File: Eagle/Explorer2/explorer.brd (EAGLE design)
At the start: 101.6 x 66 mm, 12 parts

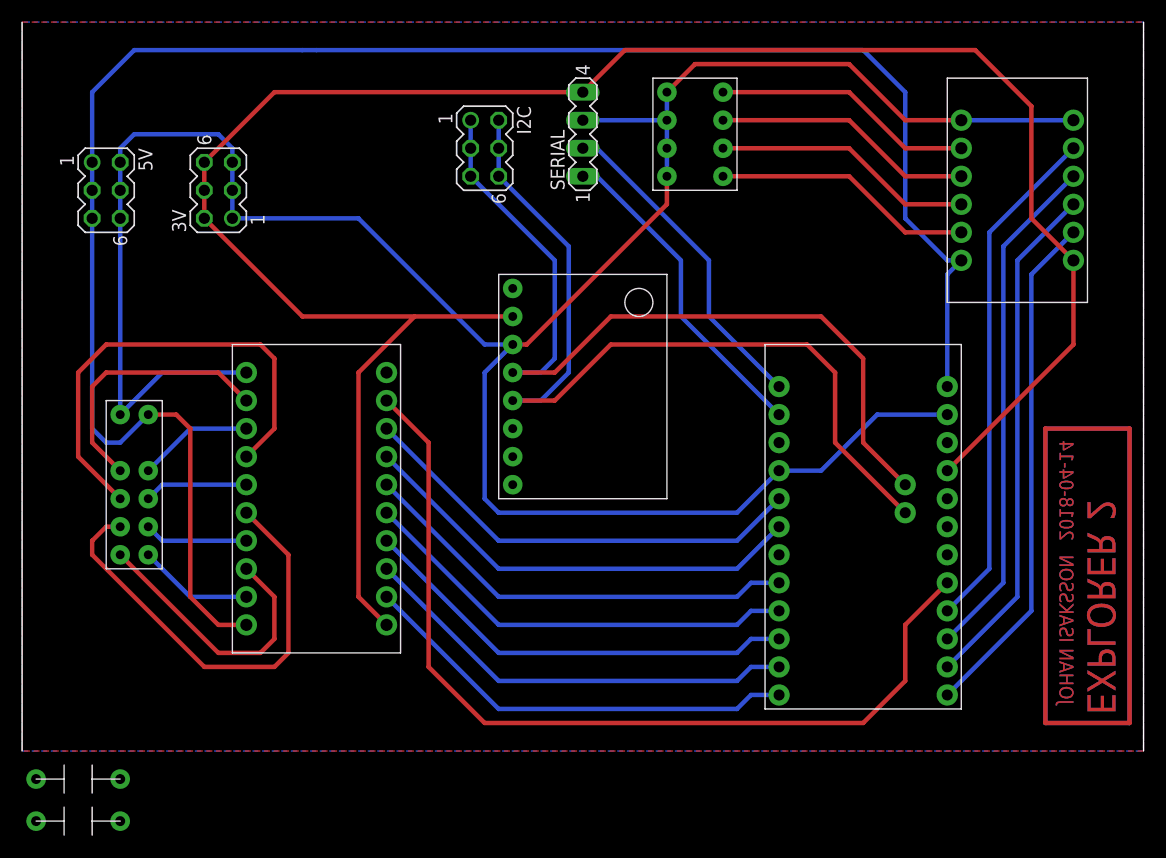
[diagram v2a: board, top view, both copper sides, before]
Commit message: Added functionality for ascending and descending in altitude hold mode.
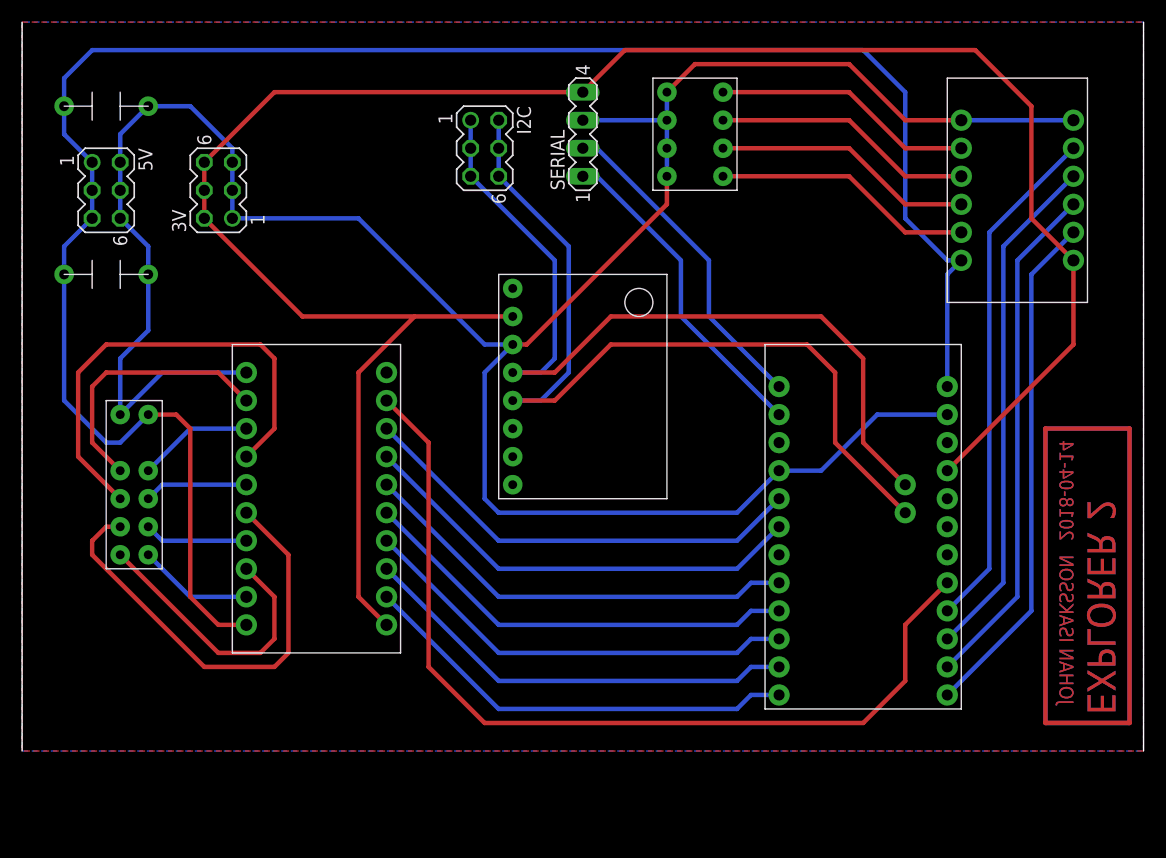
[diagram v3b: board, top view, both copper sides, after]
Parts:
- moved U$7 64.8 mm to (7.62, 58.4), turned to 180 degrees
- moved U$2 45.8 mm to (7.62, 43.2), turned to 180 degrees
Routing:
- net 5V: track 169.7 -> 176.1 mm
- net GND: track 223.0 -> 227.9 mm
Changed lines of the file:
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@@
 <element name="U$5" library="quadcopter_comp" package="LEVELSHIFT_4CH" value="LEVELSHIFT_4CH" x="90.17" y="50.8" rot="R180"/>
 <element name="U$8" library="quadcopter_comp" package="GY-86" value="GY-86" x="50.8" y="33.02"/>
-<element name="U$2" library="quadcopter_comp" package="CAP" value="CAP" x="5.08" y="-2.54"/>
-<element name="U$7" library="quadcopter_comp" package="CAP" value="CAP" x="5.08" y="-6.35"/>
+<element name="U$2" library="quadcopter_comp" package="CAP" value="CAP" x="7.62" y="43.18" rot="R180"/>
+<element name="U$7" library="quadcopter_comp" package="CAP" value="CAP" x="7.62" y="58.42" rot="R180"/>
 </elements>
 <signals>
@@
 <wire x1="74.93" y1="62.23" x2="60.96" y2="62.23" width="0.4064" layer="1"/>
 <wire x1="60.96" y1="62.23" x2="58.42" y2="59.69" width="0.4064" layer="1"/>
-<wire x1="8.89" y1="30.48" x2="8.89" y2="48.26" width="0.4064" layer="16"/>
 <wire x1="8.89" y1="50.8" x2="8.89" y2="48.26" width="0.4064" layer="16"/>
 <wire x1="8.89" y1="53.34" x2="8.89" y2="50.8" width="0.4064" layer="16"/>
@@
 <wire x1="19.05" y1="50.8" x2="19.05" y2="48.26" width="0.4064" layer="16"/>
 <wire x1="19.05" y1="53.34" x2="19.05" y2="50.8" width="0.4064" layer="16"/>
-<wire x1="8.89" y1="53.34" x2="8.89" y2="54.61" width="0.4064" layer="16"/>
-<wire x1="8.89" y1="54.61" x2="10.16" y2="55.88" width="0.4064" layer="16"/>
-<wire x1="10.16" y1="55.88" x2="17.78" y2="55.88" width="0.4064" layer="16"/>
-<wire x1="17.78" y1="55.88" x2="19.05" y2="54.61" width="0.4064" layer="16"/>
 <wire x1="19.05" y1="54.61" x2="19.05" y2="53.34" width="0.4064" layer="16"/>
 <contactref element="U$8" pad="GND"/>
@@
 <contactref element="U$2" pad="A"/>
 <contactref element="U$7" pad="A"/>
-<wire x1="1.27" y1="-2.54" x2="8.89" y2="30.48" width="0" layer="19" extent="1-1"/>
-<wire x1="1.27" y1="-6.35" x2="1.27" y2="-2.54" width="0" layer="19" extent="1-1"/>
+<wire x1="8.89" y1="53.34" x2="8.89" y2="55.88" width="0.4064" layer="16"/>
+<wire x1="8.89" y1="55.88" x2="11.43" y2="58.42" width="0.4064" layer="16"/>
+<wire x1="8.89" y1="48.26" x2="11.43" y2="45.72" width="0.4064" layer="16"/>
+<wire x1="11.43" y1="45.72" x2="11.43" y2="43.18" width="0.4064" layer="16"/>
+<wire x1="11.43" y1="43.18" x2="11.43" y2="38.1" width="0.4064" layer="16"/>
+<wire x1="11.43" y1="38.1" x2="8.89" y2="35.56" width="0.4064" layer="16"/>
+<wire x1="8.89" y1="35.56" x2="8.89" y2="30.48" width="0.4064" layer="16"/>
+<wire x1="11.43" y1="58.42" x2="15.24" y2="58.42" width="0.4064" layer="16"/>
+<wire x1="15.24" y1="58.42" x2="19.05" y2="54.61" width="0.4064" layer="16"/>
 </signal>
 <signal name="N$20">
@@
 <contactref element="5V" pad="3"/>
 <contactref element="5V" pad="5"/>
-<wire x1="76.2" y1="63.5" x2="26.67" y2="63.5" width="0.4064" layer="16"/>
-<wire x1="26.67" y1="63.5" x2="25.4" y2="63.5" width="0.4064" layer="16"/>
+<wire x1="76.2" y1="63.5" x2="6.35" y2="63.5" width="0.4064" layer="16"/>
 <wire x1="15.24" y1="29.21" x2="13.97" y2="30.48" width="0.4064" layer="1"/>
 <wire x1="13.97" y1="30.48" x2="11.43" y2="30.48" width="0.4064" layer="1"/>
@@
 <wire x1="83.82" y1="44.45" x2="80.01" y2="48.26" width="0.4064" layer="16"/>
 <wire x1="8.89" y1="27.94" x2="11.43" y2="30.48" width="0.4064" layer="16"/>
-<wire x1="6.35" y1="48.26" x2="6.35" y2="29.21" width="0.4064" layer="16"/>
-<wire x1="6.35" y1="29.21" x2="7.62" y2="27.94" width="0.4064" layer="16"/>
 <wire x1="7.62" y1="27.94" x2="8.89" y2="27.94" width="0.4064" layer="16"/>
 <wire x1="6.35" y1="48.26" x2="6.35" y2="50.8" width="0.4064" layer="16"/>
 <wire x1="6.35" y1="50.8" x2="6.35" y2="53.34" width="0.4064" layer="16"/>
-<wire x1="6.35" y1="53.34" x2="6.35" y2="59.69" width="0.4064" layer="16"/>
-<wire x1="6.35" y1="59.69" x2="10.16" y2="63.5" width="0.4064" layer="16"/>
-<wire x1="10.16" y1="63.5" x2="25.4" y2="63.5" width="0.4064" layer="16"/>
 <contactref element="U$2" pad="B"/>
 <contactref element="U$7" pad="B"/>
-<wire x1="8.89" y1="-2.54" x2="17.78" y2="11.43" width="0" layer="19" extent="1-1"/>
-<wire x1="8.89" y1="-6.35" x2="8.89" y2="-2.54" width="0" layer="19" extent="1-1"/>
+<wire x1="6.35" y1="53.34" x2="3.81" y2="55.88" width="0.4064" layer="16"/>
+<wire x1="3.81" y1="55.88" x2="3.81" y2="58.42" width="0.4064" layer="16"/>
+<wire x1="6.35" y1="48.26" x2="3.81" y2="45.72" width="0.4064" layer="16"/>
+<wire x1="3.81" y1="45.72" x2="3.81" y2="43.18" width="0.4064" layer="16"/>
+<wire x1="3.81" y1="43.18" x2="3.81" y2="31.75" width="0.4064" layer="16"/>
+<wire x1="3.81" y1="31.75" x2="7.62" y2="27.94" width="0.4064" layer="16"/>
+<wire x1="3.81" y1="58.42" x2="3.81" y2="60.96" width="0.4064" layer="16"/>
+<wire x1="3.81" y1="60.96" x2="6.35" y2="63.5" width="0.4064" layer="16"/>
 </signal>
 <signal name="3V">

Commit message: Fixed MS5611 pressure conversion.
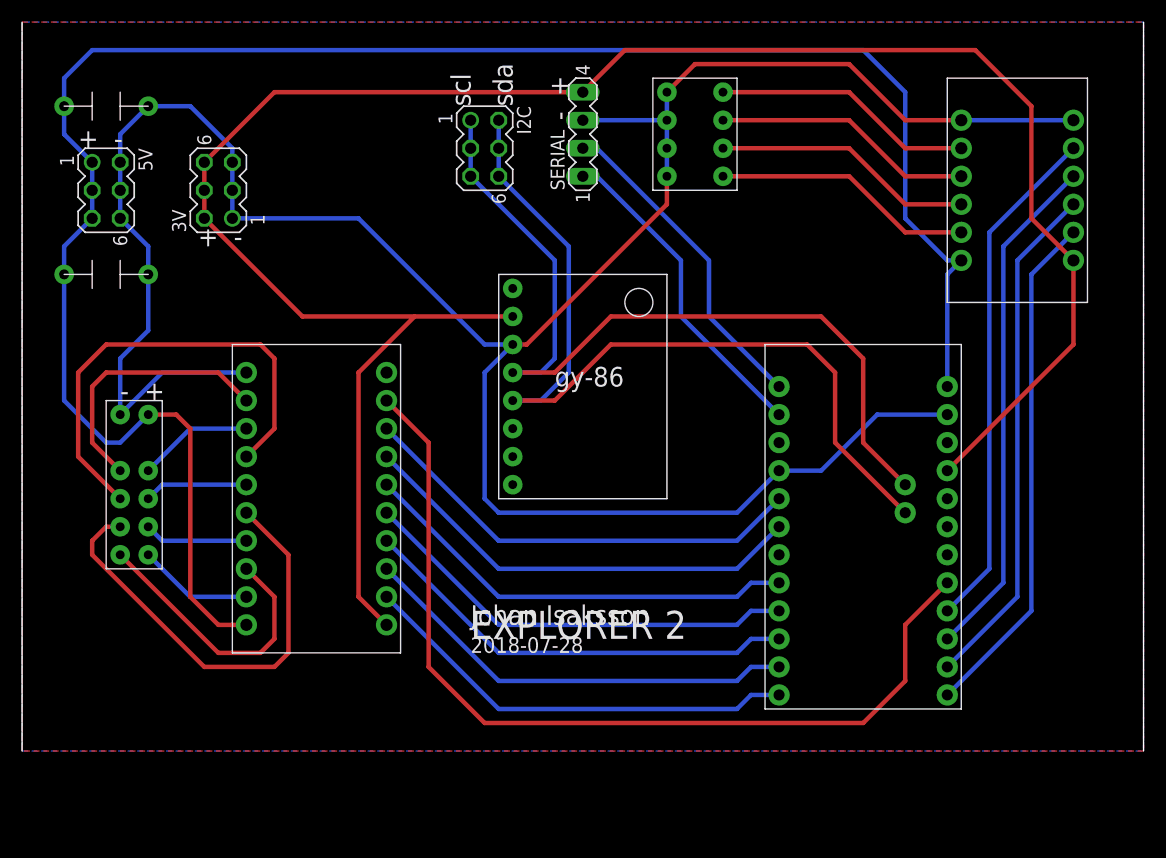
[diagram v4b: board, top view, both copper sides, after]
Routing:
- net N$29: track 68.6 -> 0.00 mm
- net N$27: track 68.6 -> 0.00 mm
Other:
- board text added: "+ -"
- board text added: "- +"
- board text added: "2018-07-28"
- board text added: "Johan Isaksson"
- board text added: "gy-86"
- board text added: "scl"
- board text added: "sda"
- board text removed: "2018-04-14"
- board text removed: "JOHAN ISAKSSON"
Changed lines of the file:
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@@
 <wire x1="101.6" y1="0" x2="101.6" y2="66.03" width="0" layer="20"/>
 <wire x1="0" y1="66.03" x2="0" y2="0" width="0" layer="20"/>
-<text x="99.06" y="22.86" size="2.54" layer="16" rot="MR270">EXPLORER 2</text>
-<text x="93.98" y="19.05" size="1.27" layer="16" rot="MR90">2018-04-14</text>
-<text x="95.25" y="17.78" size="1.27" layer="16" rot="MR270">JOHAN ISAKSSON</text>
-<text x="99.06" y="22.86" size="2.54" layer="1" rot="MR270">EXPLORER 2</text>
-<text x="93.98" y="19.05" size="1.27" layer="1" rot="MR90">2018-04-14</text>
-<text x="95.25" y="17.78" size="1.27" layer="1" rot="MR270">JOHAN ISAKSSON</text>
+<text x="48.26" y="33.02" size="1.778" layer="25">gy-86</text>
+<text x="5.08" y="54.61" size="1.778" layer="25">+  -</text>
+<text x="15.24" y="45.72" size="1.778" layer="25"> +  -</text>
+<text x="8.89" y="31.75" size="1.778" layer="25">-  +</text>
+<text x="49.53" y="57.15" size="1.778" layer="25" rot="R90">-  +</text>
+<text x="44.45" y="58.42" size="1.778" layer="25" rot="R90">sda</text>
+<text x="40.64" y="58.42" size="1.778" layer="25" rot="R90">scl</text>
+<text x="40.64" y="10.16" size="2.54" layer="25">EXPLORER 2
+</text>
+<text x="40.64" y="11.43" size="1.778" layer="25">Johan Isaksson</text>
+<text x="40.64" y="8.89" size="1.4224" layer="25">2018-07-28</text>
 </plain>
 <attributes>
@@
 <wire x1="80.01" y1="11.43" x2="83.82" y2="15.24" width="0.4064" layer="1"/>
 </signal>
-<signal name="N$27">
-<wire x1="92.71" y1="2.54" x2="92.71" y2="29.21" width="0.4064" layer="1"/>
-<wire x1="92.71" y1="29.21" x2="100.33" y2="29.21" width="0.4064" layer="1"/>
-<wire x1="100.33" y1="29.21" x2="100.33" y2="2.54" width="0.4064" layer="1"/>
-<wire x1="100.33" y1="2.54" x2="92.71" y2="2.54" width="0.4064" layer="1"/>
-</signal>
-<signal name="N$29">
-<wire x1="92.71" y1="2.54" x2="92.71" y2="29.21" width="0.4064" layer="16"/>
-<wire x1="92.71" y1="29.21" x2="100.33" y2="29.21" width="0.4064" layer="16"/>
-<wire x1="100.33" y1="29.21" x2="100.33" y2="2.54" width="0.4064" layer="16"/>
-<wire x1="100.33" y1="2.54" x2="92.71" y2="2.54" width="0.4064" layer="16"/>
-</signal>
 </signals>
 </board>
 </drawing>
+<compatibility>
+<note version="6.3" minversion="6.2.2" severity="warning">
+Since Version 6.2.2 text objects can contain more than one line,
+which will not be processed correctly with this version.
+</note>
+</compatibility>
 </eagle>
